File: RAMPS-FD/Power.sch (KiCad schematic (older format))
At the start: 19 parts, among them J101 NET-TIE, J103 NET-TIE, P101 HB_IN, P103 PS-ON, P105 12V-AUX, P107 MOT_IN, P108 POWER_IN, U3 LM7812

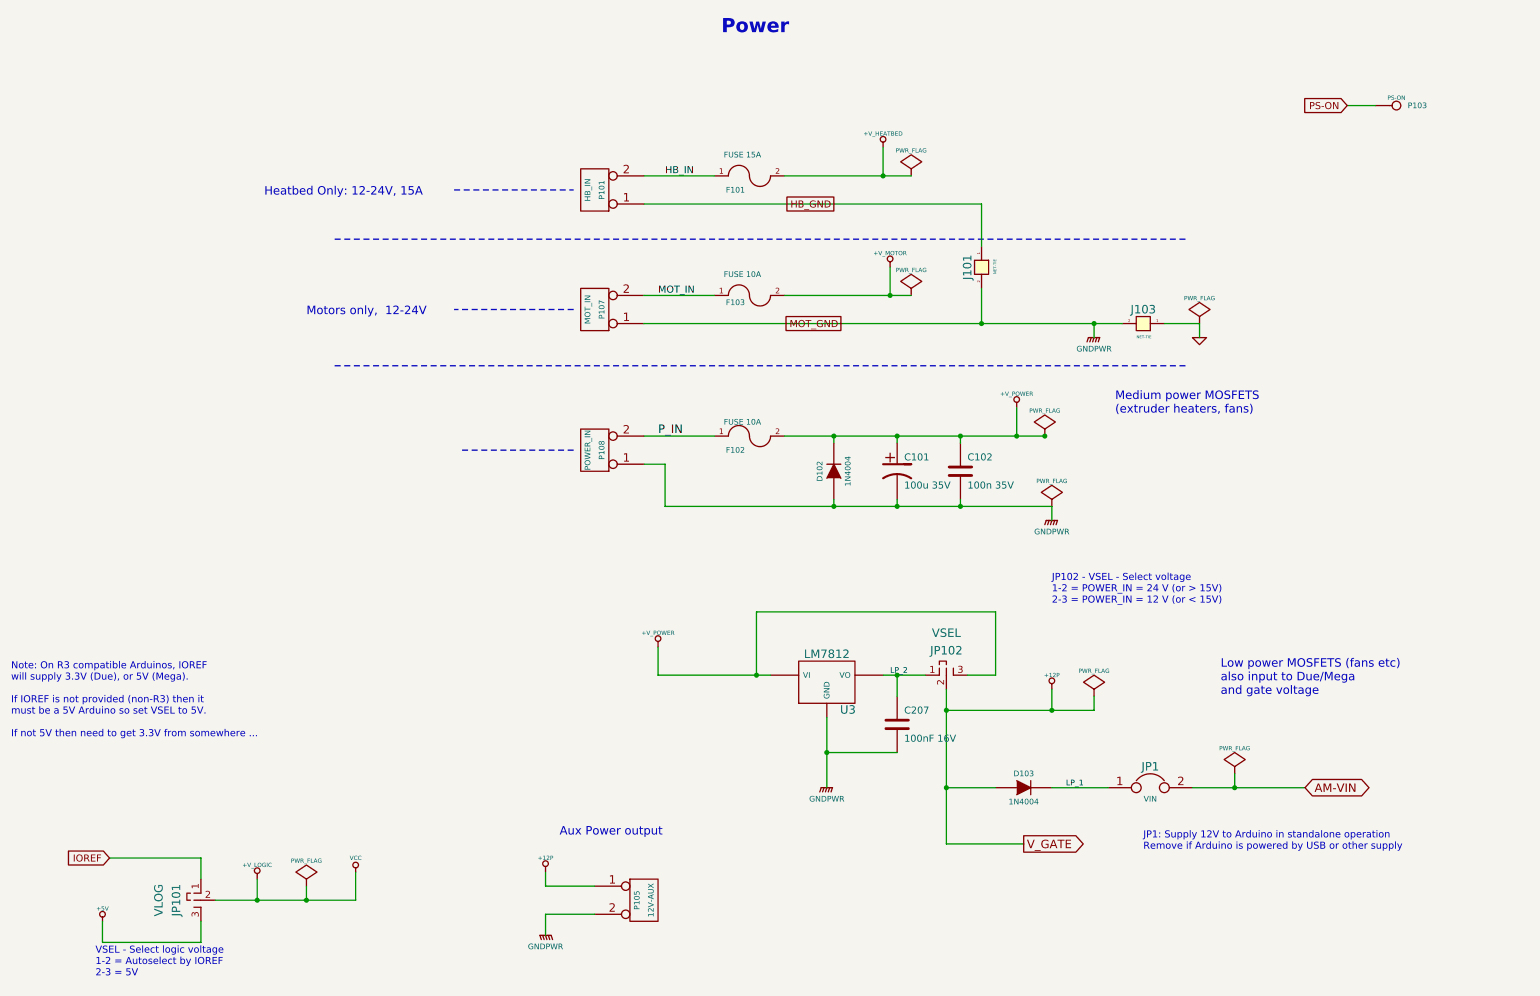
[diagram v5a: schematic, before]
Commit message: RAMPS-FD: Rev A revised
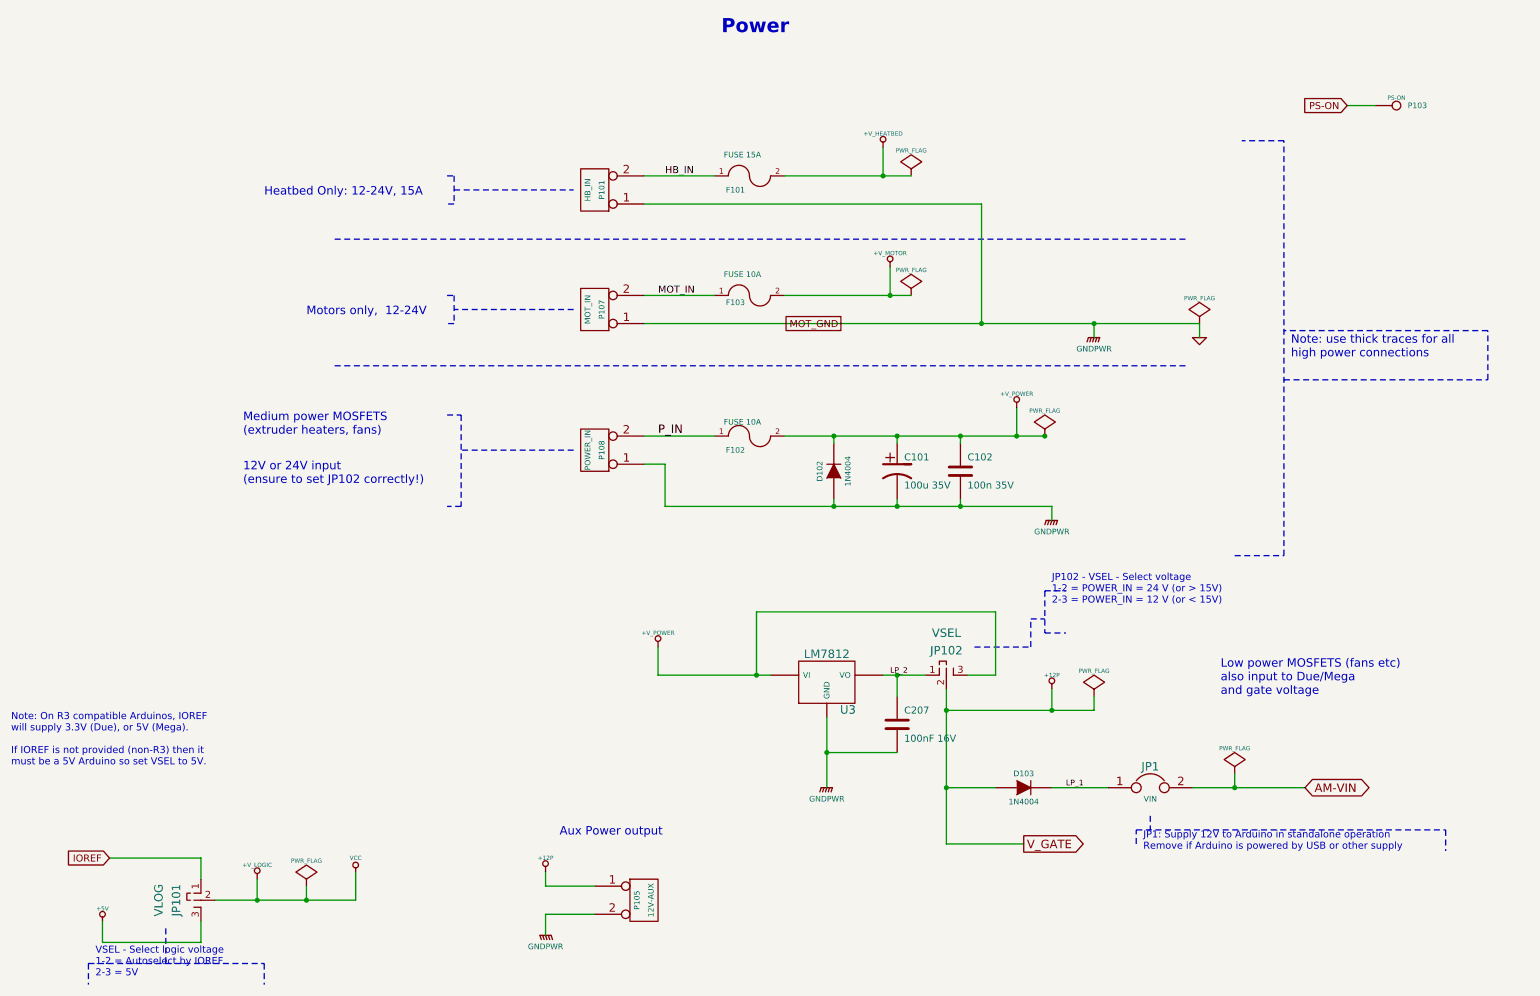
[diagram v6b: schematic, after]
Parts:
- removed J101, J103: NET-TIE, TIE-1MM, symbol NET-TIE
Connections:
- net GNDPWR is gone; now on net GND: C101.2, C102.2, C207.2, D102.1 (A), P105.2 (PM), P107.1 (P1), P108.1 (P1), U3.GND
- net HB_GND is gone; now on net GND: P101.1 (P1)
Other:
- note added: "12V or 24V input \n(ensure to set JP102 correctly!)"
- note added: "Note: On R3 compatible Arduinos, IOREF \nwill supply 3.3V (Due), or 5V (Mega).\n\nIf IOREF is not provided (non-R3) then it \nmust be a 5V Arduino so set VSEL to 5V."
- note added: "Note: use thick traces for all\nhigh power connections"
- note removed: "Note: On R3 compatible Arduinos, IOREF \nwill supply 3.3V (Due), or 5V (Mega).\n\nIf IOREF is not provided (non-R3) then it \nmust be a 5V Arduino so set VSEL to 5V.\n\nIf not 5V then need to get 3.3V from somewhere ..."
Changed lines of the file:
@@
 Sheet 2 9
 Title ""
-Date "3 oct 2013"
+Date "6 oct 2013"
 Rev ""
 Comp ""
@@
 	5250 4100 8000 4100
 Wire Wire Line
-	8800 2800 9050 2800
+	5100 2800 9050 2800
 Wire Wire Line
 	9050 2800 9050 2900
@@
 	8300 2800 8300 2900
 Wire Wire Line
-	7500 2550 7500 2800
+	7500 1950 7500 2800
 Wire Wire Line
 	5100 1750 5600 1750
@@
 Wire Wire Line
 	5100 1950 7500 1950
-Wire Wire Line
-	7500 1950 7500 2250
 Connection ~ 7500 2800
 Connection ~ 8300 2800
-Wire Wire Line
-	5100 2800 8500 2800
 Wire Wire Line
 	1950 7050 1950 7200
@@
 JP102 - VSEL - Select voltage\n1-2 = POWER_IN = 24 V (or > 15V)\n2-3 = POWER_IN = 12 V (or < 15V)
 $Comp
-L PWR_FLAG #FLG013
+L PWR_FLAG #FLG011
 U 1 1 523A3EED
 P 8300 5450
-F 0 "#FLG013" H 8300 5545 30  0001 C CNN
+F 0 "#FLG011" H 8300 5545 30  0001 C CNN
 F 1 "PWR_FLAG" H 8300 5630 30  0000 C CNN
 F 2 "" H 8300 5450 60  0001 C CNN
@@
 $EndComp
 $Comp
-L +12P #PWR014
+L +12P #PWR012
 U 1 1 523A3ECD
 P 8000 5400
-F 0 "#PWR014" H 8000 5370 30  0001 C CNN
+F 0 "#PWR012" H 8000 5370 30  0001 C CNN
 F 1 "+12P" H 8000 5500 30  0000 C CNN
 F 2 "" H 8000 5400 60  0001 C CNN
@@
 $EndComp
 $Comp
-L GNDPWR #PWR015
+L GNDPWR #PWR013
 U 1 1 523A3DBE
 P 6400 6100
-F 0 "#PWR015" H 6400 6150 40  0001 C CNN
+F 0 "#PWR013" H 6400 6150 40  0001 C CNN
 F 1 "GNDPWR" H 6400 6020 40  0000 C CNN
 F 2 "" H 6400 6100 60  0001 C CNN
@@
 $EndComp
 $Comp
-L +5V #PWR016
+L +5V #PWR014
 U 1 1 523A06E3
 P 1250 7050
-F 0 "#PWR016" H 1250 7140 20  0001 C CNN
+F 0 "#PWR014" H 1250 7140 20  0001 C CNN
 F 1 "+5V" H 1250 7140 30  0000 C CNN
 F 2 "" H 1250 7050 60  0001 C CNN
@@
 $EndComp
 $Comp
-L VCC #PWR017
+L VCC #PWR015
 U 1 1 51B4F503
 P 3050 6700
-F 0 "#PWR017" H 3050 6800 30  0001 C CNN
+F 0 "#PWR015" H 3050 6800 30  0001 C CNN
 F 1 "VCC" H 3050 6800 30  0000 C CNN
 F 2 "" H 3050 6700 60  0001 C CNN
@@
 VSEL - Select logic voltage\n1-2 = Autoselect by IOREF\n2-3 = 5V
 $Comp
-L PWR_FLAG #FLG018
+L PWR_FLAG #FLG016
 U 1 1 51AE545A
 P 9050 2800
-F 0 "#FLG018" H 9050 2895 30  0001 C CNN
+F 0 "#FLG016" H 9050 2895 30  0001 C CNN
 F 1 "PWR_FLAG" H 9050 2980 30  0000 C CNN
 F 2 "" H 9050 2800 60  0001 C CNN
@@
 $EndComp
 $Comp
-L GND #PWR019
+L GND #PWR017
 U 1 1 51AE537B
 P 9050 2900
-F 0 "#PWR019" H 9050 2900 30  0001 C CNN
+F 0 "#PWR017" H 9050 2900 30  0001 C CNN
 F 1 "GND" H 9050 2830 30  0001 C CNN
 F 2 "" H 9050 2900 60  0001 C CNN
@@
 $EndComp
 $Comp
-L GNDPWR #PWR020
+L GNDPWR #PWR018
 U 1 1 51AE535E
 P 8300 2900
-F 0 "#PWR020" H 8300 2950 40  0001 C CNN
+F 0 "#PWR018" H 8300 2950 40  0001 C CNN
 F 1 "GNDPWR" H 8300 2820 40  0000 C CNN
 F 2 "" H 8300 2900 60  0001 C CNN
@@
 HB_IN
 $Comp
-L NET-TIE J103
-U 1 1 51AA0008
-P 8700 2800
-F 0 "J103" H 8650 2900 60  0000 C CNN
-F 1 "NET-TIE" H 8655 2705 20  0000 C CNN
-F 2 "TIE-1MM" H 8610 2535 60  0001 C CNN
-F 3 "" H 8700 2800 60  0001 C CNN
-F 4 "Copper jumper block" H 8720 2420 60  0001 C CNN "Description"
-	1    8700 2800
-	1    0    0    -1
-$EndComp
-$Comp
-L GNDPWR #PWR021
+L GNDPWR #PWR019
 U 1 1 51A9FFCC
 P 4400 7150
-F 0 "#PWR021" H 4400 7200 40  0001 C CNN
+F 0 "#PWR019" H 4400 7200 40  0001 C CNN
 F 1 "GNDPWR" H 4400 7070 40  0000 C CNN
 F 2 "" H 4400 7150 60  0001 C CNN
@@
 $EndComp
 $Comp
-L GNDPWR #PWR022
+L GNDPWR #PWR020
 U 1 1 51A9FFA1
 P 8000 4200
-F 0 "#PWR022" H 8000 4250 40  0001 C CNN
+F 0 "#PWR020" H 8000 4250 40  0001 C CNN
 F 1 "GNDPWR" H 8000 4120 40  0000 C CNN
 F 2 "" H 8000 4200 60  0001 C CNN
@@
 	1    0    0    -1
 $EndComp
-Text GLabel 6450 1950 0    50   UnSpc ~ 0
-HB_GND
-$Comp
-L NET-TIE J101
-U 1 1 51A9FB93
-P 7500 2350
-F 0 "J101" H 7450 2450 60  0000 C CNN
-F 1 "NET-TIE" H 7455 2255 20  0000 C CNN
-F 2 "TIE-1MM" H 7410 2085 60  0001 C CNN
-F 3 "" H 7500 2350 60  0001 C CNN
-F 4 "Copper jumper block" H 7520 1970 60  0001 C CNN "Description"
-	1    7500 2350
-	0    -1   -1   0
-$EndComp
 Text GLabel 6500 2800 0    50   UnSpc ~ 0
 MOT_GND
-Text Notes 600  5750 0    50   ~ 0
-Note: On R3 compatible Arduinos, IOREF \nwill supply 3.3V (Due), or 5V (Mega).\n\nIf IOREF is not provided (non-R3) then it \nmust be a 5V Arduino so set VSEL to 5V.\n\nIf not 5V then need to get 3.3V from somewhere ...
-$Comp
-L PWR_FLAG #FLG023
+Text Notes 600  5950 0    50   ~ 0
+Note: On R3 compatible Arduinos, IOREF \nwill supply 3.3V (Due), or 5V (Mega).\n\nIf IOREF is not provided (non-R3) then it \nmust be a 5V Arduino so set VSEL to 5V.
+$Comp
+L PWR_FLAG #FLG021
 U 1 1 5179AAFA
 P 2700 6800
-F 0 "#FLG023" H 2700 6895 30  0001 C CNN
+F 0 "#FLG021" H 2700 6895 30  0001 C CNN
 F 1 "PWR_FLAG" H 2700 6980 30  0000 C CNN
 F 2 "" H 2700 6800 60  0001 C CNN
@@
 $EndComp
 $Comp
-L PWR_FLAG #FLG024
+L PWR_FLAG #FLG022
 U 1 1 5179AA30
 P 9300 6000
-F 0 "#FLG024" H 9300 6095 30  0001 C CNN
+F 0 "#FLG022" H 9300 6095 30  0001 C CNN
 F 1 "PWR_FLAG" H 9300 6180 30  0000 C CNN
 F 2 "" H 9300 6000 60  0001 C CNN
@@
 Text GLabel 10100 1250 0    50   Input ~ 0
 PS-ON
-Text Notes 8450 3450 0    60   ~ 0
+Text Notes 2250 3600 0    60   ~ 0
 Medium power MOSFETS \n(extruder heaters, fans)
 Text Notes 2400 1900 0    60   ~ 0
@@
 $EndComp
 $Comp
-L +V_LOGIC #PWR025
+L +V_LOGIC #PWR023
 U 1 1 517864B3
 P 2350 6750
-F 0 "#PWR025" H 2350 6720 30  0001 C CNN
+F 0 "#PWR023" H 2350 6720 30  0001 C CNN
 F 1 "+V_LOGIC" H 2350 6850 30  0000 C CNN
 F 2 "" H 2350 6750 60  0001 C CNN
@@
 $EndComp
 $Comp
-L PWR_FLAG #FLG026
+L PWR_FLAG #FLG024
 U 1 1 5176EA8B
 P 7000 2600
-F 0 "#FLG026" H 7000 2695 30  0001 C CNN
+F 0 "#FLG024" H 7000 2695 30  0001 C CNN
 F 1 "PWR_FLAG" H 7000 2780 30  0000 C CNN
 F 2 "" H 7000 2600 60  0001 C CNN
@@
 $EndComp
 $Comp
-L +V_MOTOR #PWR027
+L +V_MOTOR #PWR025
 U 1 1 5176EA85
 P 6850 2400
-F 0 "#PWR027" H 6850 2370 30  0001 C CNN
+F 0 "#PWR025" H 6850 2370 30  0001 C CNN
 F 1 "+V_MOTOR" H 6850 2500 30  0000 C CNN
 F 2 "" H 6850 2400 60  0001 C CNN
@@
 $EndComp
 $Comp
-L +V_HEATBED #PWR028
+L +V_HEATBED #PWR026
 U 1 1 5176EA3A
 P 6800 1550
-F 0 "#PWR028" H 6800 1520 30  0001 C CNN
+F 0 "#PWR026" H 6800 1520 30  0001 C CNN
 F 1 "+V_HEATBED" H 6800 1650 30  0000 C CNN
 F 2 "" H 6800 1550 60  0001 C CNN
@@
 $EndComp
 $Comp
-L +V_POWER #PWR029
+L +V_POWER #PWR027
 U 1 1 5176EA28
 P 7750 3400
-F 0 "#PWR029" H 7750 3370 30  0001 C CNN
+F 0 "#PWR027" H 7750 3370 30  0001 C CNN
 F 1 "+V_POWER" H 7750 3500 30  0000 C CNN
 F 2 "" H 7750 3400 60  0001 C CNN
@@
 $EndComp
 $Comp
-L PWR_FLAG #FLG030
+L PWR_FLAG #FLG028
 U 1 1 50FC2F79
 P 7000 1750
-F 0 "#FLG030" H 7000 1845 30  0001 C CNN
+F 0 "#FLG028" H 7000 1845 30  0001 C CNN
 F 1 "PWR_FLAG" H 7000 1930 30  0000 C CNN
 F 2 "" H 7000 1750 60  0001 C CNN
@@
 $EndComp
 $Comp
-L PWR_FLAG #FLG031
-U 1 1 50FC2F75
-P 8000 4100
-F 0 "#FLG031" H 8000 4195 30  0001 C CNN
-F 1 "PWR_FLAG" H 8000 4280 30  0000 C CNN
-F 2 "" H 8000 4100 60  0001 C CNN
-F 3 "" H 8000 4100 60  0001 C CNN
-	1    8000 4100
-	1    0    0    -1
-$EndComp
-$Comp
-L PWR_FLAG #FLG032
+L PWR_FLAG #FLG029
 U 1 1 50FC2F70
 P 7950 3600
-F 0 "#FLG032" H 7950 3695 30  0001 C CNN
+F 0 "#FLG029" H 7950 3695 30  0001 C CNN
 F 1 "PWR_FLAG" H 7950 3780 30  0000 C CNN
 F 2 "" H 7950 3600 60  0001 C CNN
@@
 	5200 5100 5200 5300
 $Comp
-L +V_POWER #PWR033
+L +V_POWER #PWR030
 U 1 1 523F90FD
 P 5200 5100
-F 0 "#PWR033" H 5200 5070 30  0001 C CNN
+F 0 "#PWR030" H 5200 5070 30  0001 C CNN
 F 1 "+V_POWER" H 5200 5200 30  0000 C CNN
 F 2 "" H 5200 5100 60  0001 C CNN
@@
 LP_2
 $Comp
-L +12P #PWR034
+L +12P #PWR031
 U 1 1 524B544A
 P 4400 6700
-F 0 "#PWR034" H 4400 6670 30  0001 C CNN
+F 0 "#PWR031" H 4400 6670 30  0001 C CNN
 F 1 "+12P" H 4400 6800 30  0000 C CNN
 F 2 "" H 4400 6700 60  0001 C CNN
@@
 	1    0    0    -1
 $EndComp
+Text Notes 9700 3050 0    60   ~ 0
+Note: use thick traces for all\nhigh power connections
+Wire Notes Line
+	9300 4450 9650 4450
+Wire Notes Line
+	9650 4450 9650 1500
+Wire Notes Line
+	9650 1500 9350 1500
+Wire Notes Line
+	9650 3200 11100 3200
+Wire Notes Line
+	11100 3200 11100 2850
+Wire Notes Line
+	11100 2850 9650 2850
+Text Notes 2250 3950 0    60   ~ 0
+12V or 24V input \n(ensure to set JP102 correctly!)
+Wire Notes Line
+	8700 6300 8700 6400
+Wire Notes Line
+	8600 6500 8600 6400
+Wire Notes Line
+	8600 6400 10800 6400
+Wire Notes Line
+	10800 6400 10800 6550
+Wire Notes Line
+	1700 7100 1700 7350
+Wire Notes Line
+	1150 7350 2400 7350
+Wire Notes Line
+	1150 7350 1150 7500
+Wire Notes Line
+	2400 7350 2400 7500
+Wire Notes Line
+	7450 5100 7850 5100
+Wire Notes Line
+	7850 5100 7850 4900
+Wire Notes Line
+	7850 4900 7950 4900
+Wire Notes Line
+	7950 4700 7950 5000
+Wire Notes Line
+	7950 4700 8100 4700
+Wire Notes Line
+	7950 5000 8100 5000
+Wire Notes Line
+	3700 1750 3750 1750
+Wire Notes Line
+	3750 1750 3750 1950
+Wire Notes Line
+	3750 1950 3700 1950
+Wire Notes Line
+	3700 2600 3750 2600
+Wire Notes Line
+	3750 2600 3750 2800
+Wire Notes Line
+	3750 2800 3700 2800
+Wire Notes Line
+	3700 3450 3800 3450
+Wire Notes Line
+	3800 3450 3800 4100
+Wire Notes Line
+	3800 4100 3700 4100
 $EndSCHEMATC

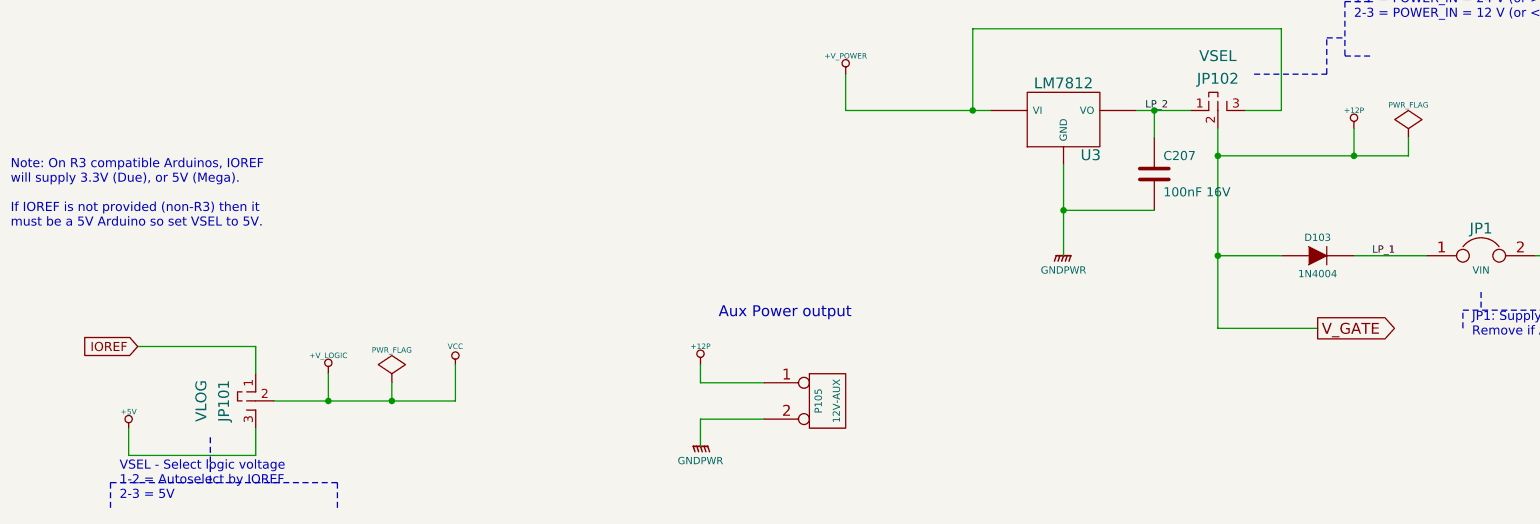
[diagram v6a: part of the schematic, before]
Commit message: RAMPS-FD schematic changes: #3 replace C301, C302, C303 and C501 with ceramic 0805; #4 change endstop connectors to 6x1 and 6x2 to allow key position #9 change E-STOP connector to KK type; #18 add 10k pulldowns on heater outputs from CPU #19 change E-STOP buffers to HCT type to always drive FETs at 5V and remove inverting drivers on heater outputs; #20 add 24LC256 I2C EEPROM
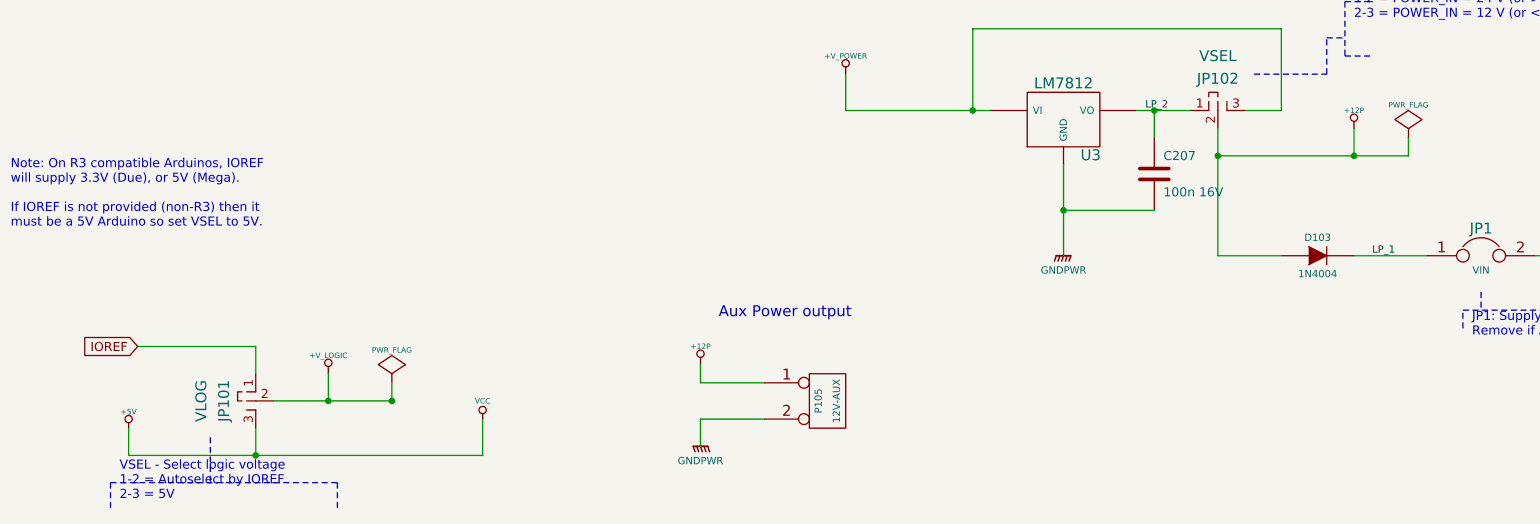
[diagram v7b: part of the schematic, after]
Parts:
- C207: value 100nF 16V -> 100n 16V
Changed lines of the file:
@@
 Sheet 2 9
 Title ""
-Date "6 oct 2013"
+Date "18 dec 2013"
 Rev ""
 Comp ""
@@
 $EndDescr
 Connection ~ 7250 5550
-Wire Wire Line
-	7250 5400 7250 6500
 Connection ~ 8000 5550
 Wire Wire Line
 	7250 5550 8300 5550
-Connection ~ 7250 6100
-Wire Wire Line
-	7250 6500 7800 6500
 Wire Wire Line
 	6800 5300 7100 5300
@@
 Connection ~ 2700 6900
 Wire Wire Line
-	2050 6900 3050 6900
+	2050 6900 2700 6900
 Wire Wire Line
 	1950 6750 1950 6600
@@
 	1950 6600 1300 6600
 Wire Wire Line
-	3050 6900 3050 6700
+	3200 7200 3200 7000
 Connection ~ 7350 4100
 Wire Wire Line
@@
 	1950 7050 1950 7200
 Wire Wire Line
-	1950 7200 1250 7200
+	1250 7200 3200 7200
 Wire Wire Line
 	1250 7200 1250 7050
 Wire Wire Line
-	2700 6800 2700 6900
+	2700 6900 2700 6800
 Wire Notes Line
 	8950 2200 2900 2200
@@
 	5200 5300 6000 5300
 Wire Wire Line
-	7600 6100 7250 6100
+	7250 6100 7600 6100
 Wire Wire Line
 	7400 5300 7600 5300
@@
 	1    0    0    -1
 $EndComp
-Text GLabel 7800 6500 2    60   Output ~ 0
-V_GATE
 $Comp
 L JUMP_MINI_3 JP102
@@
 L VCC #PWR015
 U 1 1 51B4F503
-P 3050 6700
-F 0 "#PWR015" H 3050 6800 30  0001 C CNN
-F 1 "VCC" H 3050 6800 30  0000 C CNN
-F 2 "" H 3050 6700 60  0001 C CNN
-F 3 "" H 3050 6700 60  0001 C CNN
-	1    3050 6700
+P 3200 7000
+F 0 "#PWR015" H 3200 7100 30  0001 C CNN
+F 1 "VCC" H 3200 7100 30  0000 C CNN
+F 2 "" H 3200 7000 60  0001 C CNN
+F 3 "" H 3200 7000 60  0001 C CNN
+	1    3200 7000
 	1    0    0    -1
 $EndComp
@@
 P 6900 5650
 F 0 "C207" H 6950 5750 50  0000 L CNN
-F 1 "100nF 16V" H 6950 5550 50  0000 L CNN
+F 1 "100n 16V" H 6950 5550 50  0000 L CNN
 F 2 "" H 6900 5650 60  0001 C CNN
 F 3 "" H 6900 5650 60  0001 C CNN
@@
 Wire Notes Line
 	3800 4100 3700 4100
+Wire Wire Line
+	7250 5400 7250 6100
+Connection ~ 1950 7200
 $EndSCHEMATC
